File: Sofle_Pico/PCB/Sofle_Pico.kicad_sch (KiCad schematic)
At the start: 77 parts, among them J1 Pimaroni Trackball, J2 4PIN, J3 OLED, J5 Conn_01x05_Socket, J6 Conn_01x05_Socket, SW1 SW_PUSH_LED, SW10 SW_PUSH_LED, SW11 SW_PUSH_LED, SW12 SW_PUSH_LED, SW13 SW_PUSH_LED, SW14 SW_PUSH_LED, SW15 SW_PUSH_LED, SW16 SW_PUSH_LED, SW17 SW_PUSH_LED, SW18 SW_PUSH_LED, SW19 SW_PUSH_LED, SW2 SW_PUSH_LED, SW20 SW_PUSH_LED, SW21 SW_PUSH_LED, SW22 SW_PUSH_LED, SW23 SW_PUSH_LED, SW24 SW_PUSH_LED, SW25 Rotary_Encoder_Switch, SW26 SW_PUSH_LED, SW27 SW_PUSH_LED, SW28 SW_PUSH_LED, SW29 SW_PUSH_LED, SW3 SW_PUSH_LED, SW30 SW_PUSH_LED, SW4 SW_PUSH_LED, SW5 SW_PUSH_LED, SW6 SW_PUSH_LED, SW7 SW_PUSH_LED, SW8 SW_PUSH_LED, SW9 SW_PUSH_LED, U1 SN74AHCT1G125, U3 Pico

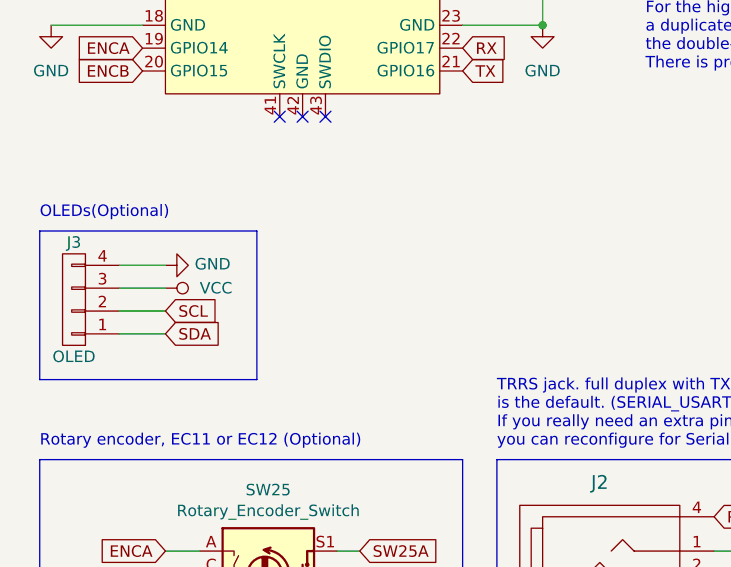
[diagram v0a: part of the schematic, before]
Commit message: Added Cirque trackpad tie in and bending jig
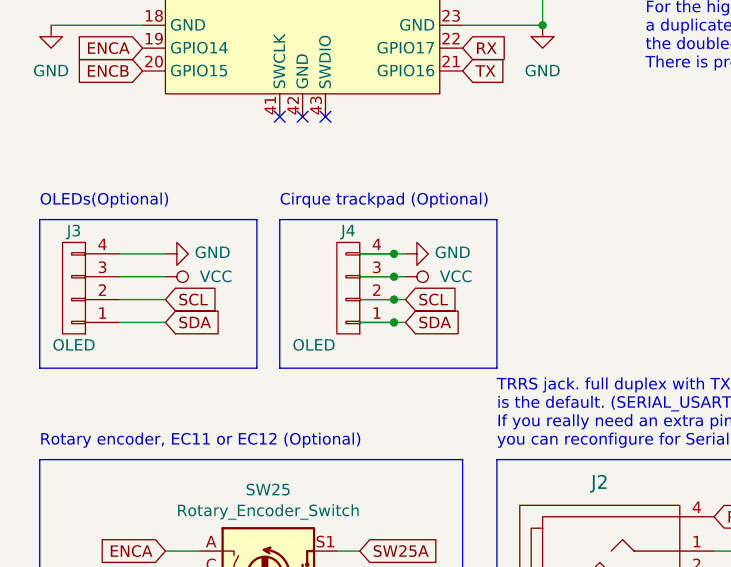
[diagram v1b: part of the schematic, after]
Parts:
- added J4: OLED, Sofle_Pico:Cirque tie in, symbol SofleKeyboard-rescue:OLED-Lily58-cache-Lily58_Pro-rescue
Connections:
- net GND: now also J4.4 (P4)
- net SCL: now also J4.2 (P2)
- net SDA: now also J4.1 (P1)
- net VCC: now also J4.3 (P3)
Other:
- note added: "Cirque trackpad (Optional)"
- moved on the sheet: J3

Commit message: Symbol consolidation and cleanup
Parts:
- J1: value Pimaroni Trackball -> Conn_01x05; symbol Connector:Conn_01x05_Socket -> Sofle_Pico:Conn_01x05
- J2: value 4PIN -> MJ-4PP-9; symbol SofleKeyboard-rescue:MJ-4PP-9-Lily58-cache-Lily58_Pro-rescue -> Sofle_Pico:MJ-4PP-9
- J3: value OLED -> Conn_01x04; symbol SofleKeyboard-rescue:OLED-Lily58-cache-Lily58_Pro-rescue -> Connector_Generic:Conn_01x04
- J4: value OLED -> Conn_01x04; symbol SofleKeyboard-rescue:OLED-Lily58-cache-Lily58_Pro-rescue -> Sofle_Pico:Conn_01x04
- J5, J6: value Conn_01x05_Socket -> Conn_01x05; symbol Connector:Conn_01x05_Socket -> Sofle_Pico:Conn_01x05
- JP1: value Level shifter bypass jumper -> Level shifter bypass jumper; symbol Jumper:SolderJumper_2_Open -> Sofle_Pico:SolderJumper_2_Open
- SW25: value Rotary_Encoder_Switch -> Rotary_Encoder_Switch-Device; symbol SofleKeyboard-rescue:Rotary_Encoder_Switch-Device -> Sofle_Pico:Rotary_Encoder_Switch-Device
- TH1, TH2, TH3, TH4, TH5, TH6, TH7, TH8: symbol SofleKeyboard-rescue:HOLE-Lily58-cache-Lily58_Pro-rescue -> Sofle_Pico:MountingHole
- U1: footprint Sofle_Pico:SN74AHCT1G125 - Junco -> Sofle_Pico:SN74AHCT1G125; symbol Junco:SN74AHCT1G125 -> Sofle_Pico:SN74AHCT1G125

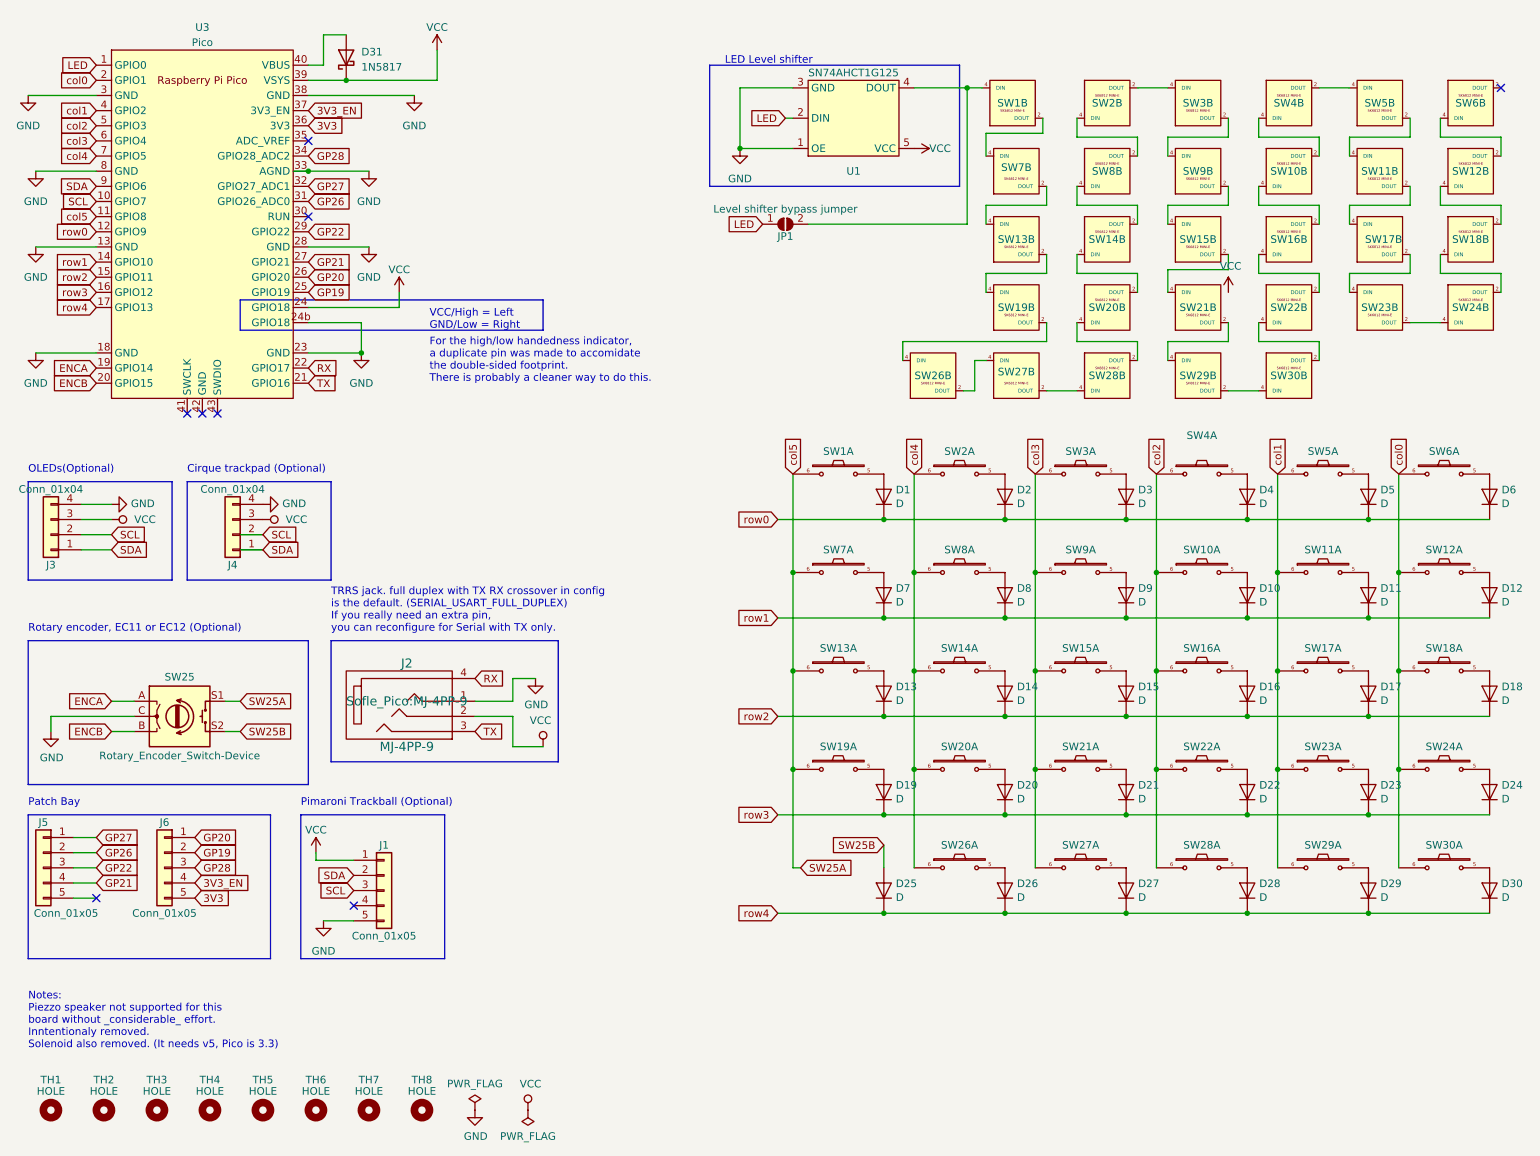
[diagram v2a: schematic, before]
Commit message: Refactored to seperate switch & LED
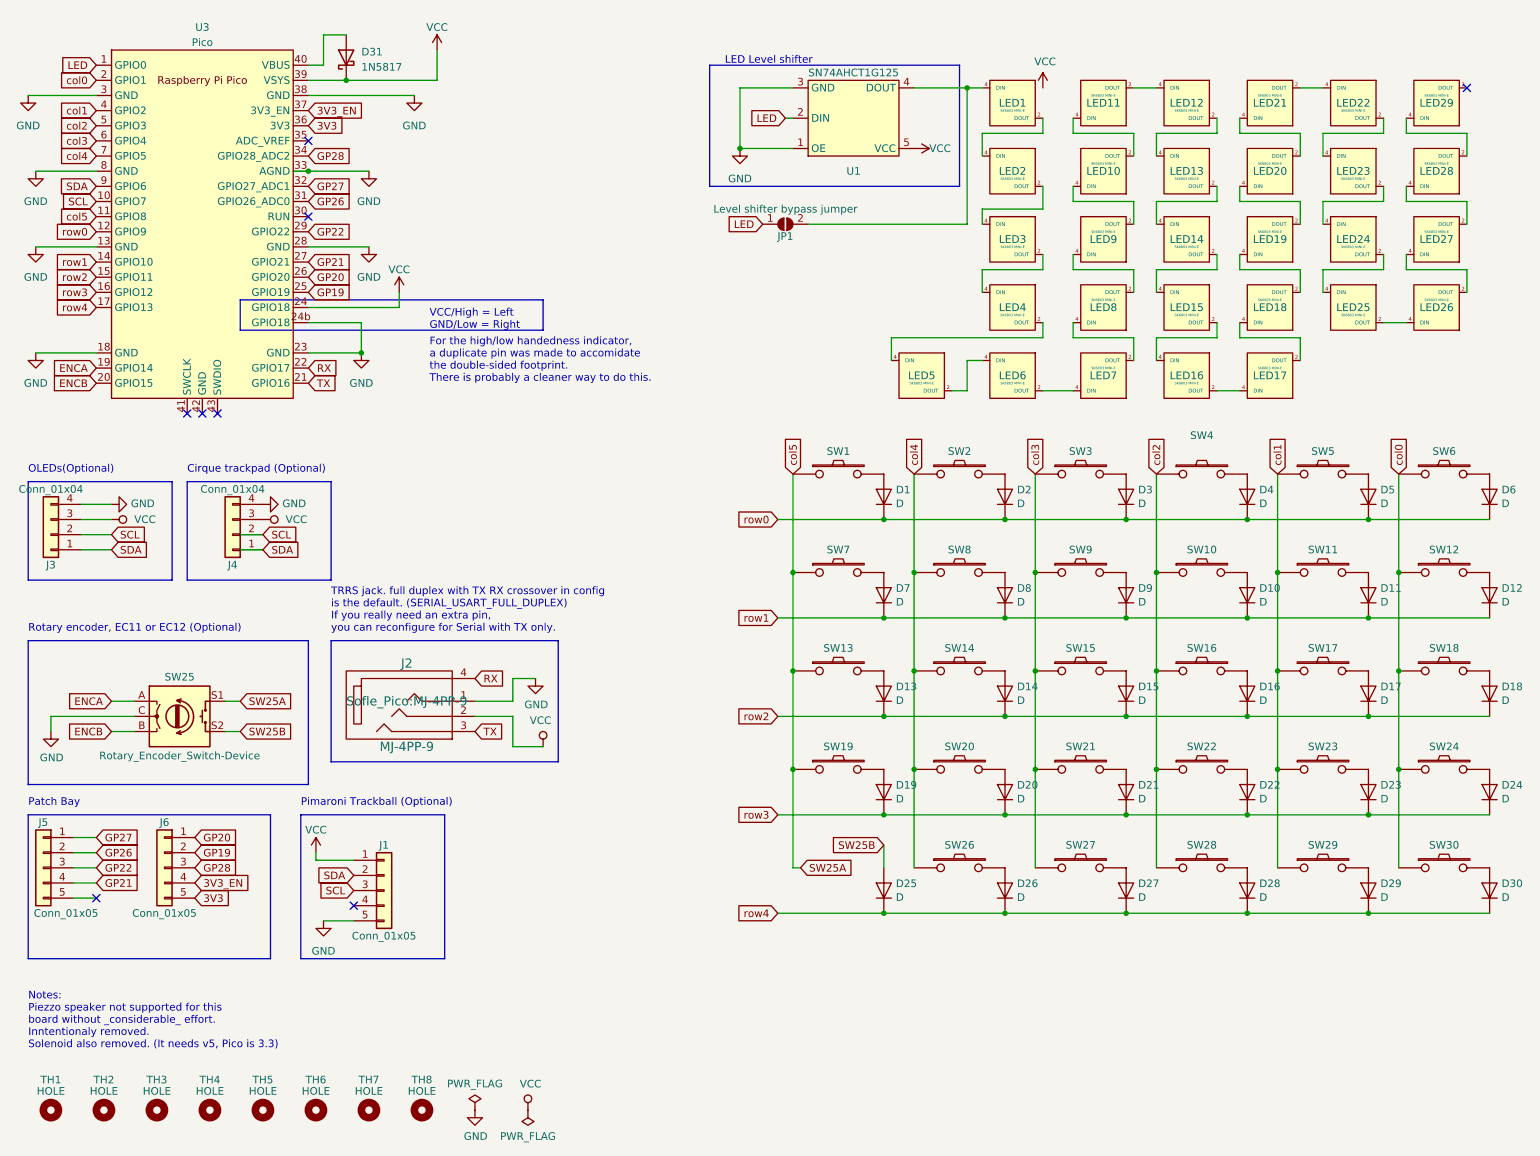
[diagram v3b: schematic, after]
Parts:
- removed unit 2 of SW1
- removed unit 2 of SW10
- removed unit 2 of SW11
- removed unit 2 of SW12
- removed unit 2 of SW13
- removed unit 2 of SW14
- removed unit 2 of SW15
- removed unit 2 of SW16
- removed unit 2 of SW17
- removed unit 2 of SW18
- removed unit 2 of SW19
- removed unit 2 of SW2
- removed unit 2 of SW20
- removed unit 2 of SW21
- removed unit 2 of SW22
- removed unit 2 of SW23
- removed unit 2 of SW24
- removed unit 2 of SW26
- removed unit 2 of SW27
- removed unit 2 of SW28
- removed unit 2 of SW29
- removed unit 2 of SW3
- removed unit 2 of SW30
- removed unit 2 of SW4
- removed unit 2 of SW5
- removed unit 2 of SW6
- removed unit 2 of SW7
- removed unit 2 of SW8
- removed unit 2 of SW9
- added LED1, LED10, LED11, LED12, LED13, LED14, LED15, LED16, LED17, LED18, LED19, LED2, LED20, LED21, LED22, LED23, LED24, LED25, LED26, LED27, LED28, LED29, LED3, LED4, LED5, LED6, LED7, LED8, LED9: SK6803 MINI-E, Sofle_Pico:SK6803_MINIE_v3.5.4, symbol Sofle_Pico:SK6803MINIE
- SW1, SW10, SW11, SW12, SW13, SW14, SW15, SW16, SW17, SW18, SW19, SW2, SW20, SW21, SW22, SW23, SW24, SW26, SW27, SW28, SW29, SW3, SW30, SW4, SW5, SW6, SW7, SW8, SW9: footprint Sofle_Pico:Cherry_MX_DS_Hotswap_miniE_1U_v3.5.2 -> Sofle_Pico:Cherry_MX_DS_Hotswap_v3.5.4; symbol SofleKeyboard:SW_PUSH_LED -> Sofle_Pico:SW_PUSH
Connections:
- net GND: now also LED1.3 (GND), LED10.3 (GND), LED11.3 (GND), LED12.3 (GND), LED13.3 (GND), LED14.3 (GND), LED15.3 (GND), LED16.3 (GND), LED17.3 (GND), LED18.3 (GND), LED19.3 (GND), LED2.3 (GND), LED20.3 (GND), LED21.3 (GND), LED22.3 (GND), LED23.3 (GND), LED24.3 (GND), LED25.3 (GND), LED26.3 (GND), LED27.3 (GND), LED28.3 (GND), LED29.3 (GND), LED3.3 (GND), LED4.3 (GND), LED5.3 (GND), LED6.3 (GND), LED7.3 (GND), LED8.3 (GND), LED9.3 (GND)
- net SW25A: now also SW1.1, SW13.1, SW19.1, SW7.1; no longer SW1.6, SW13.6, SW19.6, SW7.6
- net VCC: now also LED1.1 (VDD), LED10.1 (VDD), LED11.1 (VDD), LED12.1 (VDD), LED13.1 (VDD), LED14.1 (VDD), LED15.1 (VDD), LED16.1 (VDD), LED17.1 (VDD), LED18.1 (VDD), LED19.1 (VDD), LED2.1 (VDD), LED20.1 (VDD), LED21.1 (VDD), LED22.1 (VDD), LED23.1 (VDD), LED24.1 (VDD), LED25.1 (VDD), LED26.1 (VDD), LED27.1 (VDD), LED28.1 (VDD), LED29.1 (VDD), LED3.1 (VDD), LED4.1 (VDD), LED5.1 (VDD), LED6.1 (VDD), LED7.1 (VDD), LED8.1 (VDD), LED9.1 (VDD)
- net col0: now also SW12.1, SW18.1, SW24.1, SW30.1, SW6.1; no longer SW12.6, SW18.6, SW24.6, SW30.6, SW6.6
- net col1: now also SW11.1, SW17.1, SW23.1, SW29.1, SW5.1; no longer SW11.6, SW17.6, SW23.6, SW29.6, SW5.6
- net col2: now also SW10.1, SW16.1, SW22.1, SW28.1, SW4.1; no longer SW10.6, SW16.6, SW22.6, SW28.6, SW4.6
- net col3: now also SW15.1, SW21.1, SW27.1, SW3.1, SW9.1; no longer SW15.6, SW21.6, SW27.6, SW3.6, SW9.6
- net col4: now also SW14.1, SW2.1, SW20.1, SW26.1, SW8.1; no longer SW14.6, SW2.6, SW20.6, SW26.6, SW8.6
- net at D26.2 (A): now also SW26.2; no longer SW26.5
- net at D1.2 (A): now also SW1.2; no longer SW1.5
- net at D2.2 (A): now also SW2.2; no longer SW2.5
- net at D3.2 (A): now also SW3.2; no longer SW3.5
- net at D4.2 (A): now also SW4.2; no longer SW4.5
- net at D5.2 (A): now also SW5.2; no longer SW5.5
- net at D6.2 (A): now also SW6.2; no longer SW6.5
- net at D8.2 (A): now also SW8.2; no longer SW8.5
- net at D9.2 (A): now also SW9.2; no longer SW9.5
- net at D10.2 (A): now also SW10.2; no longer SW10.5
- net at D11.2 (A): now also SW11.2; no longer SW11.5
- net at D12.2 (A): now also SW12.2; no longer SW12.5
- net at D7.2 (A): now also SW7.2; no longer SW7.5
- net at D13.2 (A): now also SW13.2; no longer SW13.5
- net at D14.2 (A): now also SW14.2; no longer SW14.5
- net at D15.2 (A): now also SW15.2; no longer SW15.5
- net at D16.2 (A): now also SW16.2; no longer SW16.5
- net at D17.2 (A): now also SW17.2; no longer SW17.5
- net at D18.2 (A): now also SW18.2; no longer SW18.5
- net at D21.2 (A): now also SW21.2; no longer SW21.5
- net at D22.2 (A): now also SW22.2; no longer SW22.5
- net at D23.2 (A): now also SW23.2; no longer SW23.5
- net at D24.2 (A): now also SW24.2; no longer SW24.5
- net at D20.2 (A): now also SW20.2; no longer SW20.5
- net at D19.2 (A): now also SW19.2; no longer SW19.5
- net at D27.2 (A): now also SW27.2; no longer SW27.5
- net at D28.2 (A): now also SW28.2; no longer SW28.5
- net at D29.2 (A): now also SW29.2; no longer SW29.5
- net at D30.2 (A): now also SW30.2; no longer SW30.5
- net at JP1.2 (B), U1.4 (DOUT): now also LED1.4 (DIN)
- new net: LED5.2 (DOUT), LED6.4 (DIN)
- new net: LED4.2 (DOUT), LED5.4 (DIN)
- new net: LED28.2 (DOUT), LED29.4 (DIN)
- new net: LED2.2 (DOUT), LED3.4 (DIN)
- new net: LED1.2 (DOUT), LED2.4 (DIN)
- new net: LED17.2 (DOUT), LED18.4 (DIN)
- new net: LED16.2 (DOUT), LED17.4 (DIN)
- new net: LED13.2 (DOUT), LED14.4 (DIN)
- new net: LED12.2 (DOUT), LED13.4 (DIN)
- new net: LED10.2 (DOUT), LED11.4 (DIN)
- new net: LED10.4 (DIN), LED9.2 (DOUT)
- new net: LED23.2 (DOUT), LED24.4 (DIN)
- new net: LED22.2 (DOUT), LED23.4 (DIN)
- new net: LED15.2 (DOUT), LED16.4 (DIN)
- new net: LED7.2 (DOUT), LED8.4 (DIN)
- new net: LED6.2 (DOUT), LED7.4 (DIN)
- new net: LED8.2 (DOUT), LED9.4 (DIN)
- new net: LED11.2 (DOUT), LED12.4 (DIN)
- new net: LED26.2 (DOUT), LED27.4 (DIN)
- new net: LED25.2 (DOUT), LED26.4 (DIN)
- new net: LED24.2 (DOUT), LED25.4 (DIN)
- new net: LED27.2 (DOUT), LED28.4 (DIN)
- new net: LED18.2 (DOUT), LED19.4 (DIN)
- new net: LED20.2 (DOUT), LED21.4 (DIN)
- new net: LED19.2 (DOUT), LED20.4 (DIN)
- new net: LED21.2 (DOUT), LED22.4 (DIN)
- new net: LED3.2 (DOUT), LED4.4 (DIN)
- new net: LED14.2 (DOUT), LED15.4 (DIN)
